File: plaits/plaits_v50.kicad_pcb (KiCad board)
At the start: 2 copper layers, 61.2 x 99.9 mm, 149 parts, among them IC1 TLC59281DBQ, J1 Conn_01x04_Male, J10 AudioJack3_Ground, J11 AudioJack3_Ground, J12 AudioJack3_Ground, J13 AudioJack3_Ground, J14 AudioJack3_Ground, J2 Conn_01x02_Male, J3 Conn_01x02_Male, J4 AudioJack3_Ground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

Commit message: Modified the eurorackpin schematic and cleaned up
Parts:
- added C61: 1uF, Capacitor_SMD:C_0402_1005Metric, B.Cu at (148.2, 87.9)
- added D12: LM4040DBZ-10, Package_TO_SOT_SMD:SOT-23, B.Cu at (148.7, 93.2)
- added R44: 2.2k, Resistor_SMD:R_0402_1005Metric, B.Cu at (147.2, 87.9)
- moved D5 10.8 mm to (96.0, 78.2), turned to 0 degrees
- moved L2 10.4 mm to (143.3, 75.6), turned to 0 degrees
- moved D4 2.79 mm to (96.1, 75.1)
- moved L1 0.40 mm to (143.4, 84.2)
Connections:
- C12 pad 2: +3V3_A -> +3.3VA
- C14 pad 1: +3V3_A -> +3.3VA
- C20 pad 1: AREF_-10 -> VEE
- C31 pad 2: VCC -> 12Vto5V
- C32 pad 2: VCC -> 12Vto5V
- C38 pad 2: +3V3_A -> +3.3VA
- C39 pad 1: +3V3_A -> +3.3VA
- C40 pad 1: +3V3_A -> +3.3VA
- C41 pad 2: +3V3_A -> +3.3VA
- C42 pad 2: +3V3_A -> +3.3VA
- C43 pad 1: +3V3_A -> +3.3VA
- C44 pad 1: +3V3_A -> +3.3VA
- C6 pad 2: AREF_-10 -> VEE
- C8 pad 2: AREF_-10 -> VEE
- C9 pad 2: +3V3_A -> +3.3VA
- D4 pad 1: VCC -> 12Vto5V
- D4 pad 2: GND -> 12VC
- D5 pad 1: GND -> -12VC
- D5 pad 2: AREF_-10 -> Net-(D5-Pad2)
- L1 pad 1: 12VC -> 12Vto5V
- L2 pad 1: -12VC -> Net-(D5-Pad2)
- L2 pad 2: AREF_-10 -> VEE
- RV1 pad 1: +3V3_A -> +3.3VA
- RV2 pad 1: +3V3_A -> +3.3VA
- RV3 pad 1: +3V3_A -> +3.3VA
- RV4 pad 1: +3V3_A -> +3.3VA
- RV5 pad 1: +3V3_A -> +3.3VA
- RV6 pad 1: +3V3_A -> +3.3VA
- RV7 pad 1: +3V3_A -> +3.3VA
- U1 pad 8: +3V3_A -> +3.3VA
- U2 pad 4: AREF_-10 -> VEE
- U3 pad 1: VCC -> 12Vto5V
- U4 pad 2: +3V3_A -> +3.3VA
- U4 pad 3: VCC -> 12Vto5V
- U5 pad 24: +3V3_A -> +3.3VA
- U5 pad 9: +3V3_A -> +3.3VA
- U6 pad 4: +3V3_A -> +3.3VA
- U7 pad 4: +3V3_A -> +3.3VA
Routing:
- net VCC: track 66.8 -> 0.00 mm
- net AREF_-10: track 54.4 -> 0.00 mm
- net +3V3_A: track 44.8 -> 3.84 mm
- net +3.3VA: track 0.00 -> 41.0 mm
- net 12Vto5V: track 0.00 -> 4.25 mm
- net -12VC: track 5.72 -> 2.54 mm
- net 12VC: track 5.71 -> 2.54 mm

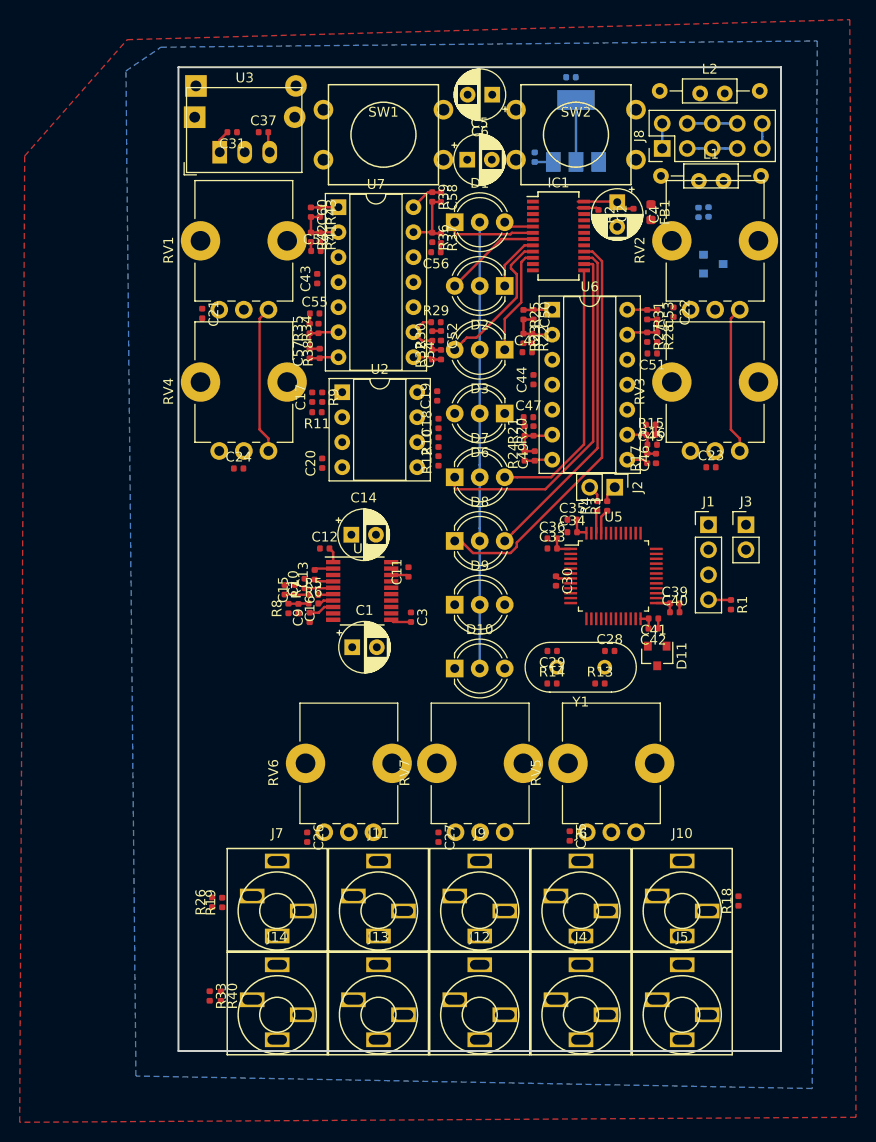
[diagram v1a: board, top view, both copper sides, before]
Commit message: Added yarns midi eurorack
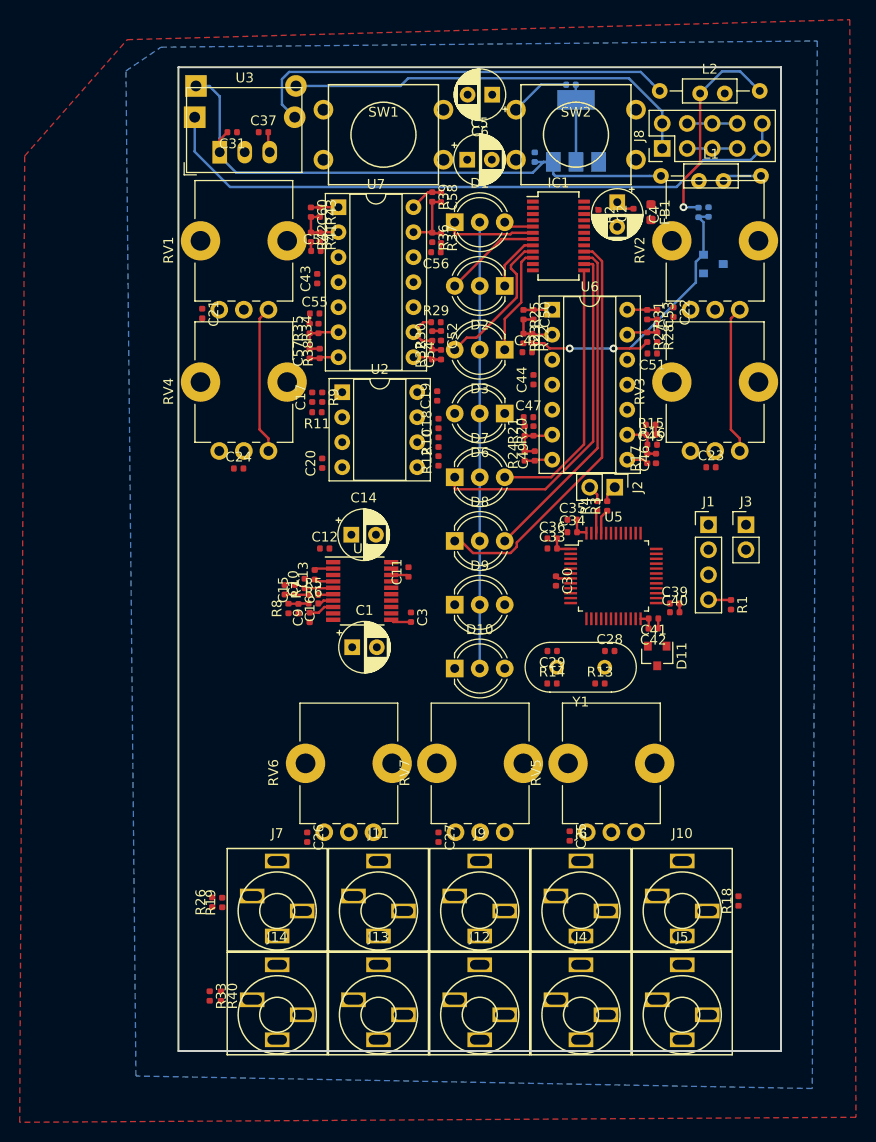
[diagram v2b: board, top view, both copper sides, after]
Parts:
- moved C38 0.76 mm to (134.2, 74.9)
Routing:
- net -12VC: track 2.54 -> 66.8 mm
- net 12Vto5V: track 4.25 -> 60.5 mm
- net Net-(D5-Pad2): track 0.00 -> 43.9 mm
- net 12VC: track 2.54 -> 42.7 mm
- net AREF_-10: track 0.00 -> 31.5 mm, vias 0 -> 2
- net VEE: track 0.00 -> 21.6 mm, vias 0 -> 1
- net GND: track 12.1 -> 18.2 mm
- net VCC: track 0.00 -> 4.02 mm
- net Net-(C2-Pad2): track 5.95 -> 2.01 mm
- net +3V3_A: track 3.84 -> 0.00 mm
- net Net-(IC1-Pad23): track 2.19 -> 0.30 mm
- net +3.3VA: track 41.0 -> 42.5 mm
